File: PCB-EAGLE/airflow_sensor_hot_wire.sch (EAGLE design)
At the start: 42 parts, among them J5 POWER_JACK, Q2 200mA/40V, U2 BME280, U4 BME280

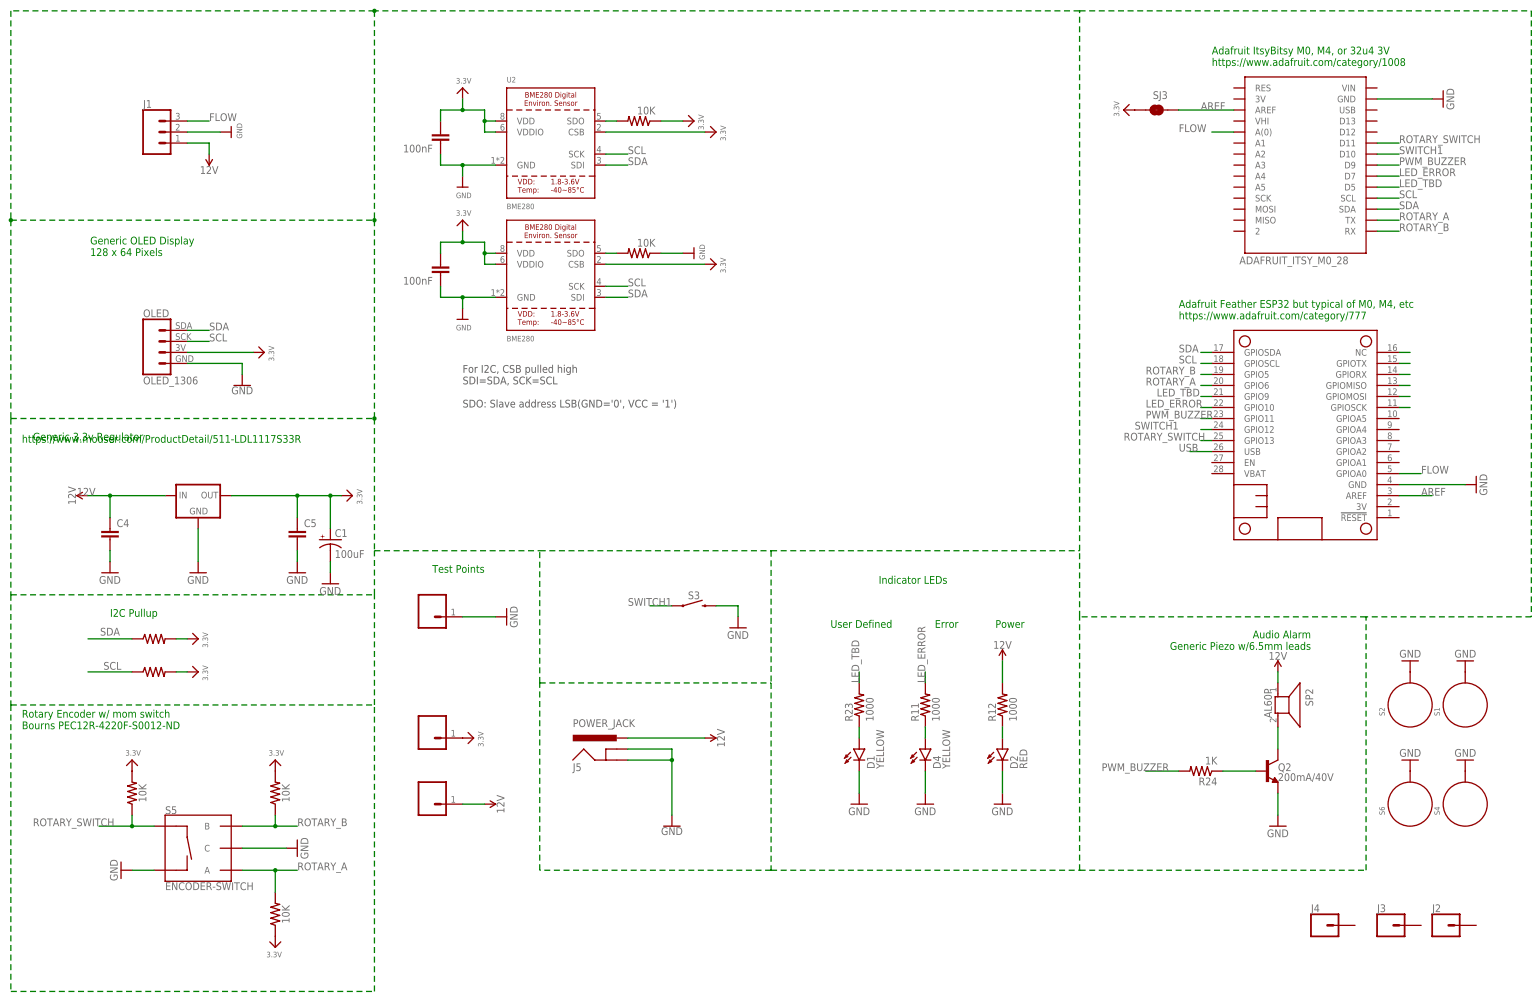
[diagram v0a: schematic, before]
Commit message: schematic update
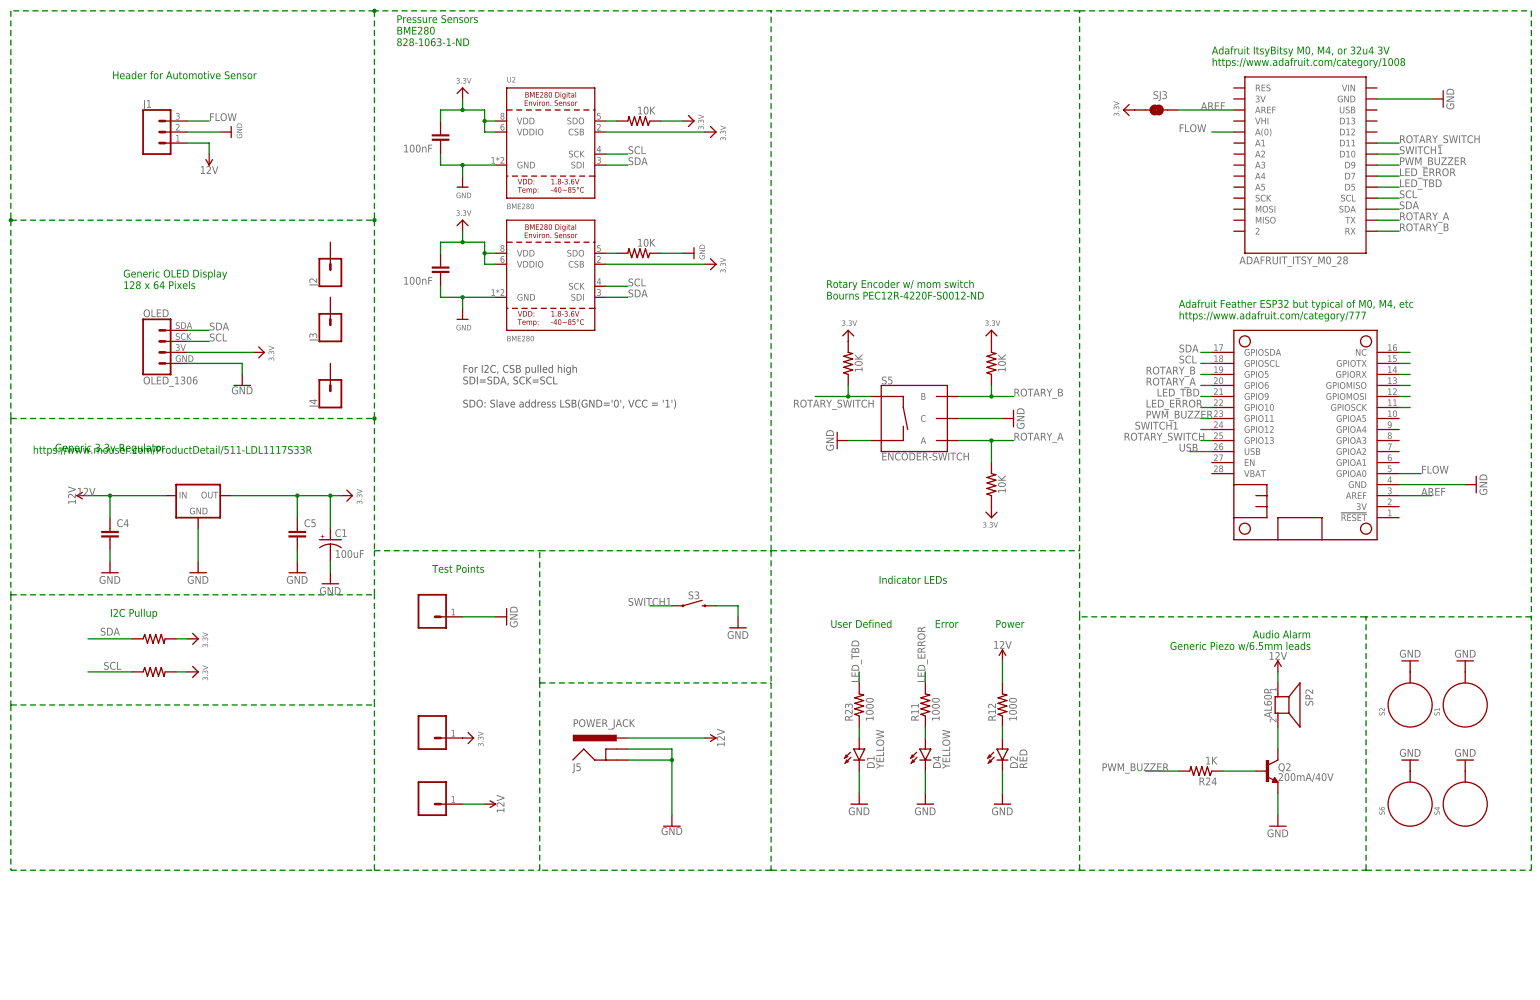
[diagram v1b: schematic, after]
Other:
- note added: "Header for Automotive Sensor"
- note added: "Pressure Sensors BME280 828-1063-1-ND"
- moved on the sheet: J2, J3, J4, S5
